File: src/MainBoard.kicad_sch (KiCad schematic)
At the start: 75 parts, among them J10 1217080-1, J11 1217080-1, J12 1217080-1, J13 1217080-1, J14 1217080-1, J15 1217080-1, J16 1217080-1, J4 MiniFit_2x08_F, J5 1217080-1, J6 1217080-1, J7 1217080-1, J8 1217080-1, J9 1217080-1, K1 RAYEX-L90S, K2 LR2A-12W, K3 LR2A-12W, Q1 BC547, Q10 2N7002, Q3 2N7002, Q4 2N7002, Q5 2N7002, Q6 2N7002, Q7 BC547, Q8 BC557, Q9 2N7002, U1 ATtiny85-20P

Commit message: Update schematics
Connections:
- new net: A1.6 (SS), A2.6 (SS)
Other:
- moved on the sheet: D4, D6, Q3, Q4, R?

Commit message: update Schematics
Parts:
- removed A1: MP2307DN_3A_Master, symbol Modules:MP2307DN_3A
- removed A2: MP2307DN_3A_Slave, symbol Modules:MP2307DN_3A
- removed A3: MP2307DN_3A, symbol Modules:MP2307DN_3A
- removed BT1: 8.4V, symbol Device:Battery_Cell
- removed C4, C5: 1µF, symbol Device:C_Polarized
- removed C6, C7: 2200µF, symbol Device:C_Polarized
- removed C? (x2): 120µF, Capacitor_THT:C_Disc_D5.0mm_W2.5mm_P5.00mm, symbol Device:C
- removed C?: 100nF, Capacitor_THT:C_Disc_D5.0mm_W2.5mm_P5.00mm, symbol Device:C
- removed D25, D8: US1M, Diode_SMD:D_SMA, symbol Diode:US1M
- removed D26, D6, D7: BZX79C2V7, Diode_SMD:D_MiniMELF, symbol Diode:BZV55C2V7
- removed F?: 12V 5A, symbol Device:Fuse
- removed F?: 12V 30A, symbol Device:Fuse
- removed F?: 12V 20A, symbol Device:Fuse
- removed F?: 12V 15A, symbol Device:Fuse
- removed F?: 12V 10A, symbol Device:Fuse
- removed F?: 5V 5A, symbol Device:Fuse
- removed J10, J11, J12, J13, J14, J15, J16, J5, J6, J7, J8, J9: 1217080-1, 1217080-1, symbol SamacSys_Parts:1217080-1
- removed J4: MiniFit_2x08_F, Connector_Molex:Molex_Mini-Fit_Jr_5566-16A_2x08_P4.20mm_Vertical, symbol Connector_Generic:Conn_02x08_Counter_Clockwise
- removed J?: Barrel_Jack, Connector_BarrelJack:BarrelJack_CUI_PJ-063AH_Horizontal, symbol Connector:Barrel_Jack
- removed J?: XT60-M, Connector_AMASS:AMASS_XT60PW-M_1x02_P7.20mm_Horizontal, symbol Connector:Conn_01x02_Pin
- removed J?: XT60L-F, Connector_AMASS:AMASS_XT60-M_1x02_P7.20mm_Vertical, symbol Connector:Conn_01x02_Pin
- removed K1: RAYEX-L90S, Relay_THT:Relay_SPDT_RAYEX-L90S, symbol Relay:RAYEX-L90S
- removed K2: LR2A-12W, SamacSys_Parts:AZ9431CH12DE, symbol Local Components:LR2A-12W
- removed K3: LR2A-12W, Relay_THT:Relay_SPDT_Finder_36.11, symbol Local Components:LR2A-12W
- removed L1, L2: 100µH, symbol Device:L_Ferrite
- removed Q1, Q7: BC547, Package_TO_SOT_THT:TO-92_Inline, symbol Transistor_BJT:BC547
- removed Q3, Q6: 2N7002, Package_TO_SOT_SMD:SOT-23, symbol Transistor_FET:2N7002
- removed Q8: BC557, Package_TO_SOT_THT:TO-92_Inline, symbol Transistor_BJT:BC557
- removed Q?: BPW96B, LED_THT:LED_D5.0mm, symbol Device:Q_Photo_NPN
- removed R? (x7): 10K, Resistor_SMD:R_1206_3216Metric_Pad1.30x1.75mm_HandSolder, symbol Device:R
- removed R? (x2): 33K, Resistor_SMD:R_1206_3216Metric_Pad1.30x1.75mm_HandSolder, symbol Device:R
- removed R?: 1K, Resistor_THT:R_Axial_DIN0204_L3.6mm_D1.6mm_P5.08mm_Horizontal, symbol Device:R
- removed R?: 1M, Resistor_SMD:R_1206_3216Metric_Pad1.30x1.75mm_HandSolder, symbol Device:R
- removed RV2: 47K, symbol Device:R_Potentiometer
- removed U1: ATtiny85-20P, Package_DIP:DIP-8_W7.62mm, symbol MCU_Microchip_ATtiny:ATtiny85-20P
- added C1: 10nF, symbol Device:C_Polarized
- added C2: 100nF, symbol Device:C_Polarized
- added D11, D7: P600A, Diode_THT:D_P600_R-6_P12.70mm_Horizontal, symbol Device:D
- added D23, D31, D32, D33, D5, D8: BZX79C2V7, Diode_SMD:D_MiniMELF, symbol Diode:BZV55C2V7
- added D6: US1M, Diode_SMD:D_SMA, symbol Diode:US1M
- added J3: MiniFit_2x10_F, symbol Connector_Generic:Conn_02x10_Counter_Clockwise
- added J69: 1217080-1, 1217080-1, symbol SamacSys_Parts:1217080-1
- added J?: XT60-M, Connector_AMASS:AMASS_XT60PW-M_1x02_P7.20mm_Horizontal, symbol Connector:Conn_01x02_Pin
- added J?: XT60L-F, Connector_AMASS:AMASS_XT60-M_1x02_P7.20mm_Vertical, symbol Connector:Conn_01x02_Pin
- added K4 (x2): FINDER-40.61, Relay_THT:Relay_DPDT_Finder_40.52, symbol Relay:FINDER-40.51
- added Q1, Q11, Q13, Q2: 2N7002, Package_TO_SOT_SMD:SOT-23, symbol Transistor_FET:2N7002
- added Q12, Q3: BS250, Package_TO_SOT_THT:TO-92_Inline, symbol Transistor_FET:BS250
- added R? (x7): 10K, Resistor_SMD:R_1206_3216Metric_Pad1.30x1.75mm_HandSolder, symbol Device:R
- added R?: 1K, Resistor_SMD:R_1206_3216Metric_Pad1.30x1.75mm_HandSolder, symbol Device:R
- added U1: LM555xN, Package_DIP:DIP-8_W7.62mm, symbol Timer:LM555xN
- RV1: value 100K -> 10K-50K
- renumbered D5 to D12
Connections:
- net +5V: now also J3.6 (Pin_6), R?.2, U1.8 (VCC); no longer RV1.1
- net +BATT: now also J3.7 (Pin_7), Q12.1 (D), Q3.1 (D); no longer D3.1 (K)
- net +VDC: now also J?.2 (Pin_2), J?.2 (Pin_2)
- net GND: now also C1.2, C2.2, D23.2 (A), D31.2 (A), D33.2 (A), D5.2 (A), D8.2 (A), J69.1, J69.2, J?.1 (Pin_1), J?.1 (Pin_1), K4.12, K4.12, Q1.2 (S), Q11.2 (S), Q13.2 (S), Q2.2 (S), U1.1 (GND); no longer D10.2 (A), D2.2 (A), D9.2 (A), Q10.2 (S), Q9.2 (S), RV1.3
- net GNDDash: now also Q10.2 (S), J3.8 (Pin_8)
- net Key: now also J3.1 (Pin_1)
- net LowBat: now also J3.10 (Pin_10)
- net PLight: now also J3.9 (Pin_9), R?.1
- net VInst: now also J3.3 (Pin_3)
- net VLight: now also J3.5 (Pin_5), K4.14, K4.14
- net VOutlet: now also J3.4 (Pin_4)
- net VRadio: now also J3.2 (Pin_2)
- net at Q4.1 (G): now also D8.1 (K), Q3.2 (G), R?.2
- net at Q4.3 (D): now also Q3.3 (S), R?.1
- net PLightSignal: now reaches Q10.1 (G)
- net PLightSignal: now also D32.1 (K), Q12.2 (G), Q13.1 (G), R?.2, U1.4 (R)
- net at Q9.1 (G): now also D23.1 (K), R?.2; no longer Q10.3 (D)
- net AuxHBeam: now reaches D3.2 (A)
- net AuxHBeam: now also J3.13 (Pin_13), K4.11
- net at D12.1 (K), Q5.1 (G), R?.2: now also R?.2
- net at RV1.2: now also C2.1, U1.2 (TR), U1.6 (THR)
- net at D4.1 (K): now also Q1.1 (G), R?.2
- net at D1.2 (A): now also K4.A2, Q1.3 (D)
- net HazardLed: now reaches Q9.3 (D)
- net HazardLed: now also J3.17 (Pin_17), Q11.3 (D)
- net +5VA renamed AuxSwitch
- net AuxSwitch: now also J3.16 (Pin_16), K4.A1, K4.A1
- net AuxSwitch1: no longer names the net of D9.1 (K)
- net AuxSwitch1: now also RV1.3
- net AuxSwitch2: no longer names the net of D10.1 (K)
- net AuxSwitch2: now also D9.2 (A), R?.1, U1.7 (DIS)
- net DimmerDash: no longer names the net of R?.1
- net DimmerDash: now also R?.1, U1.3 (Q)
- new net: D2.2 (A), K4.A2, Q2.3 (D)
- new net: D32.2 (A), D33.1 (K)
- new net: Q12.3 (S), Q13.3 (D), R?.1
- new net: D31.1 (K), Q11.1 (G), R?.2
- new net: D5.1 (K), Q2.1 (G), R?.2
- new net: C1.1, U1.5 (CV)
- new net: D10.2 (A), RV1.1
- new net: Q10.3 (D), Q9.2 (S)
- new net AuxBeams: D3.1 (K), D6.1 (K), J3.15 (Pin_15)
- new net AuxLBeam: D6.2 (A), J3.11 (Pin_11), K4.11
- new net HBeam: J3.14 (Pin_14), R?.1
- new net Hazard: D11.2 (A), D7.2 (A), J3.18 (Pin_18), R?.1
- new net LBeam: J3.12 (Pin_12), R?.1
- new net LBlinker: D11.1 (K), J3.19 (Pin_19)
- new net RBlinker: D7.1 (K), J3.20 (Pin_20)
- no-connect marks 4 -> 0
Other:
- added sheet Power Delivery (FuseBox.kicad_sch)
- note added: "Common Ground"
- note added: "Hazard signal"
- note added: "Main Power"
- note removed: "12DC Outlet"
- note removed: "CLC Choke"
- note removed: "Fuse Box"
- note removed: "Low Battery meter (Set trigger at > 11.5V)"
- note removed: "Main Power and Kill switch"
- note removed: "Radio backup battery"
- note removed: "Voltage Regulator (5V, 6A Max) Remove FB, SS and Comp circuitry from Slave module Jumper wire both modules chip"
- moved on the sheet: D12, Q5, R?

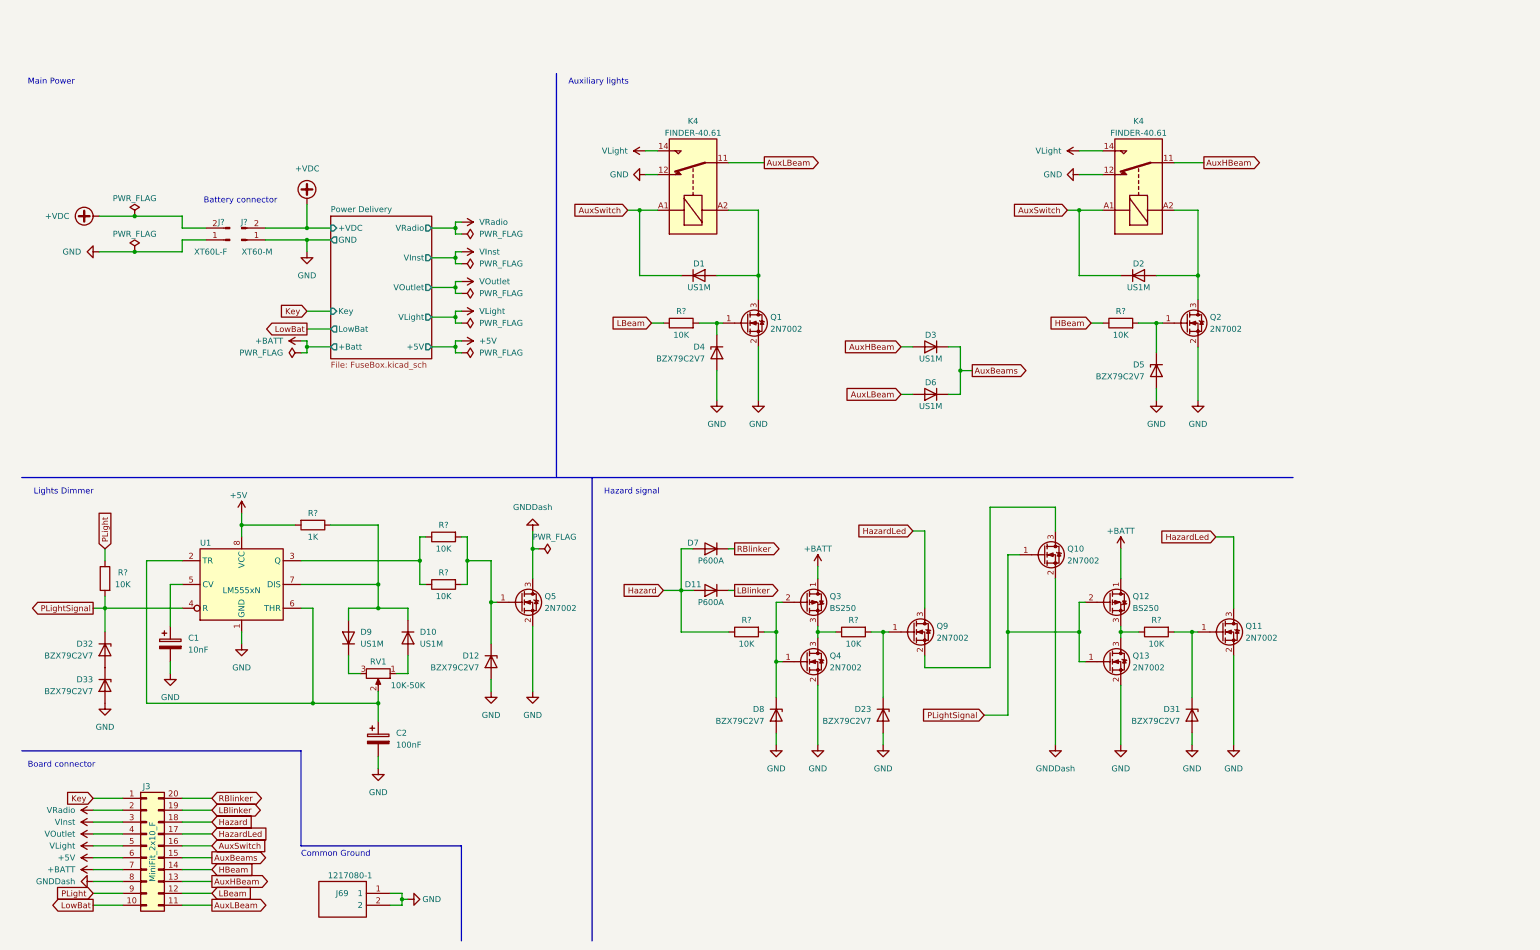
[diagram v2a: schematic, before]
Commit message: Update Schmatics; Cleanup unecessary circuits; Simplify blinkers dimmers; Update PCB; Colorize motorcycle electric diagram.
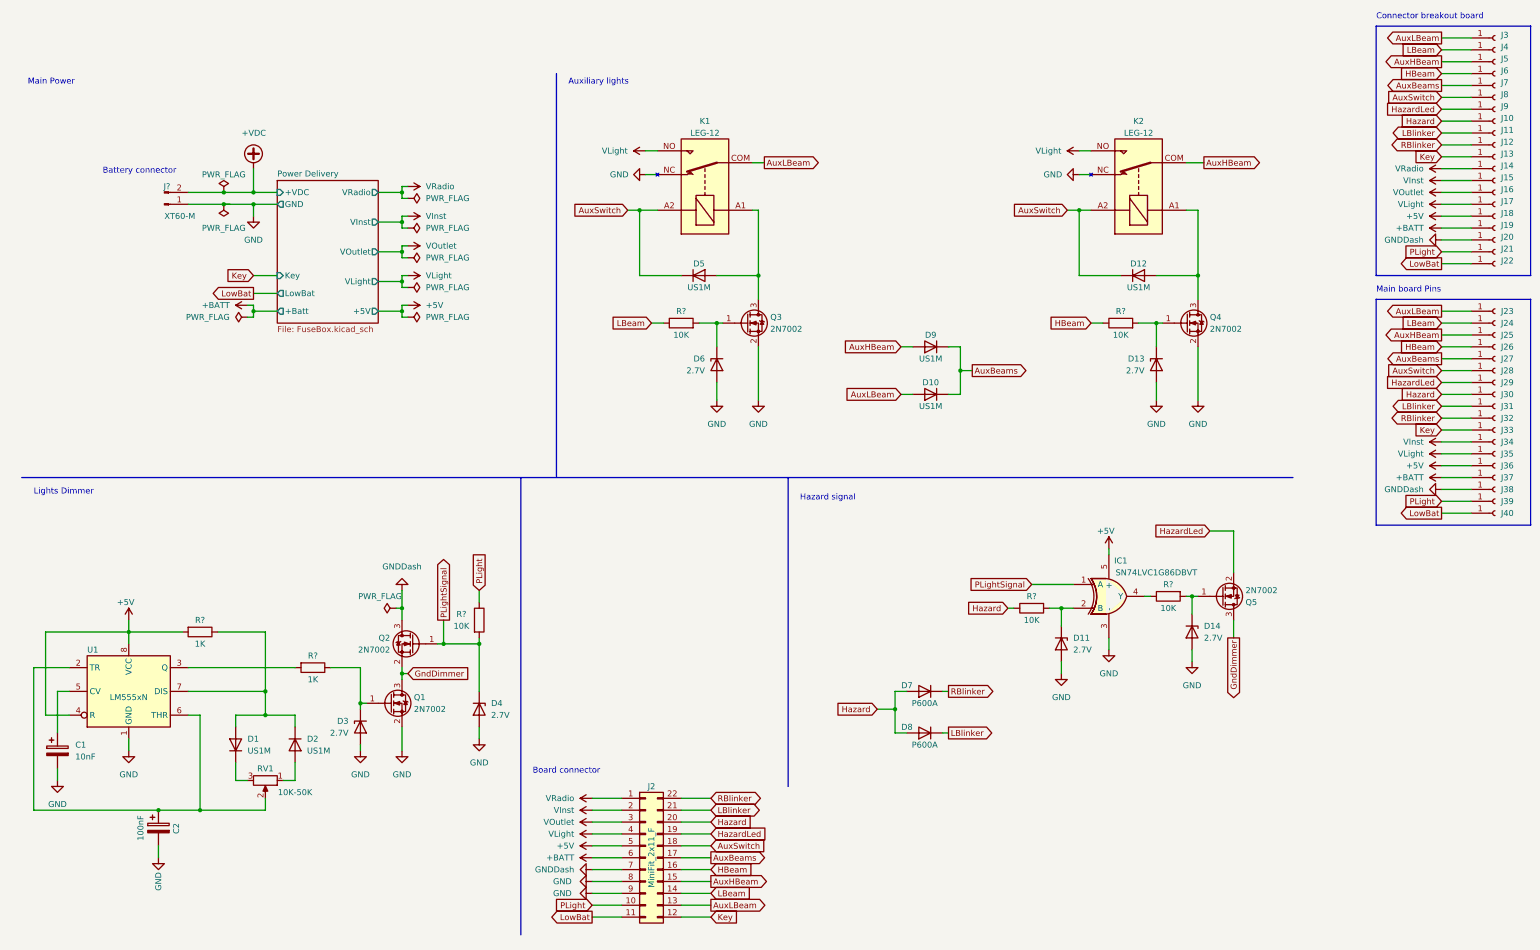
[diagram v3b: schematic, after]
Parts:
- removed D12, D23, D31, D32, D33, D5, D8: BZX79C2V7, Diode_SMD:D_MiniMELF, symbol Diode:BZV55C2V7
- removed J3: MiniFit_2x10_F, symbol Connector_Generic:Conn_02x10_Counter_Clockwise
- removed J69: 1217080-1, 1217080-1, symbol SamacSys_Parts:1217080-1
- removed J?: XT60L-F, Connector_AMASS:AMASS_XT60-M_1x02_P7.20mm_Vertical, symbol Connector:Conn_01x02_Pin
- removed K4 (x2): FINDER-40.61, Relay_THT:Relay_DPDT_Finder_40.52, symbol Relay:FINDER-40.51
- removed Q10, Q11, Q13, Q4, Q9: 2N7002, Package_TO_SOT_SMD:SOT-23, symbol Transistor_FET:2N7002
- removed Q12, Q3: BS250, Package_TO_SOT_THT:TO-92_Inline, symbol Transistor_FET:BS250
- removed R? (x5): 10K, Resistor_SMD:R_1206_3216Metric_Pad1.30x1.75mm_HandSolder, symbol Device:R
- added D11, D13, D14, D3, D4: 2.7V, Diode_SMD:D_MiniMELF, symbol Diode:BZV55C2V7
- added IC1: SN74LVC1G86DBVT, SOT95P280X145-5N, symbol Local Components:SN74LVC1G86DBVT
- added J10, J11, J12, J13, J14, J15, J16, J17, J18, J19, J20, J21, J22, J23, J24, J25, J26, J27, J28, J29, J3, J30, J31, J32, J33, J34, J35, J36, J37, J38, J39, J4, J40, J5, J6, J7, J8, J9: Conn_01x01_Socket, Connector_Pin:Pin_D1.0mm_L10.0mm, symbol Connector:Conn_01x01_Socket
- added J2: MiniFit_2x11_F, symbol Connector_Generic:Conn_02x11_Counter_Clockwise
- added K1, K2: LEG-12, Local Footprints:LEG12, symbol Local Components:LEG-12
- added Q2, Q5: 2N7002, Package_TO_SOT_SMD:SOT-23, symbol Transistor_FET:2N7002
- added R?: 1K, Resistor_SMD:R_1206_3216Metric_Pad1.30x1.75mm_HandSolder, symbol Device:R
- added R? (x2): 10K, Resistor_SMD:R_1206_3216Metric_Pad1.30x1.75mm_HandSolder, symbol Device:R
- D6: renamed from D4; value BZX79C2V7 -> 2.7V
- J?: footprint Connector_AMASS:AMASS_XT60PW-M_1x02_P7.20mm_Horizontal -> Local Footprints:AMASS_XT60PW-M_1x02_P7.20mm_Horizontal_Short
- renumbered D9 to D1, D6 to D10, D2 to D12, D10 to D2, D1 to D5, D11 to D8, D3 to D9, Q5 to Q1, Q1 to Q3, Q2 to Q4
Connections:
- net +5V: now also U1.4 (R), IC1.5 (+), J18.1 (Pin_1), J2.5 (Pin_5), J36.1 (Pin_1)
- net +BATT: now also J19.1 (Pin_1), J2.6 (Pin_6), J37.1 (Pin_1)
- net AuxBeams: now also J2.17 (Pin_17), J27.1 (Pin_1), J7.1 (Pin_1)
- net AuxHBeam: now also J2.15 (Pin_15), J25.1 (Pin_1), J5.1 (Pin_1), K2.COM
- net AuxLBeam: now also J2.13 (Pin_13), J23.1 (Pin_1), J3.1 (Pin_1), K1.COM
- net AuxSwitch: now also J2.18 (Pin_18), J28.1 (Pin_1), J8.1 (Pin_1), K1.A2, K2.A2
- net GND: now also D11.2 (A), D13.2 (A), D14.2 (A), D3.2 (A), D4.2 (A), IC1.3 (-), J2.8 (Pin_8), J2.9 (Pin_9), K1.NC, K2.NC
- net GNDDash: now also J2.7 (Pin_7), J20.1 (Pin_1), J38.1 (Pin_1), Q2.3 (D); no longer Q1.3 (D)
- net HBeam: now also J2.16 (Pin_16), J26.1 (Pin_1), J6.1 (Pin_1)
- net Hazard: now also J10.1 (Pin_1), J2.20 (Pin_20), J30.1 (Pin_1), R?.1
- net HazardLed: now also J2.19 (Pin_19), J29.1 (Pin_1), J9.1 (Pin_1), Q5.2 (S)
- net Key: now also J13.1 (Pin_1), J2.12 (Pin_12), J33.1 (Pin_1)
- net LBeam: now also J2.14 (Pin_14), J24.1 (Pin_1), J4.1 (Pin_1)
- net LBlinker: now also J11.1 (Pin_1), J2.21 (Pin_21), J31.1 (Pin_1)
- net LowBat: now also J2.11 (Pin_11), J22.1 (Pin_1), J40.1 (Pin_1)
- net PLight: now also J2.10 (Pin_10), J21.1 (Pin_1), J39.1 (Pin_1)
- net PLightSignal: now also D4.1 (K), IC1.1 (A), Q2.1 (G); no longer U1.4 (R)
- net RBlinker: now also J12.1 (Pin_1), J2.22 (Pin_22), J32.1 (Pin_1)
- net VInst: now also J15.1 (Pin_1), J2.2 (Pin_2), J34.1 (Pin_1)
- net VLight: now also J17.1 (Pin_1), J2.4 (Pin_4), J35.1 (Pin_1), K1.NO, K2.NO
- net VOutlet: now also J16.1 (Pin_1), J2.3 (Pin_3)
- net VRadio: now also J14.1 (Pin_1), J2.1 (Pin_1)
- net at D12.2 (A), Q4.3 (D): now also K2.A1
- net at U1.3 (Q): now also R?.2
- net at Q1.1 (G): now also D3.1 (K), R?.1
- net at Q4.1 (G), R?.2: now also D13.1 (K)
- net at D5.2 (A), Q3.3 (D): now also K1.A1
- new net: D14.1 (K), Q5.1 (G), R?.2
- new net: D11.1 (K), IC1.2 (B), R?.2
- new net: IC1.4 (Y), R?.1
- new net GndDimmer: Q1.3 (D), Q2.2 (S), Q5.3 (D)
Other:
- note added: "Connector breakout board"
- note added: "Main board Pins"
- note removed: "Common Ground"
- moved on the sheet: C1, C2, D1, D2, D6, D7, D8, J?, Q1, R?, RV1, U1

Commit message: Update Schematics; Replace xor with quad nand; Update PCB
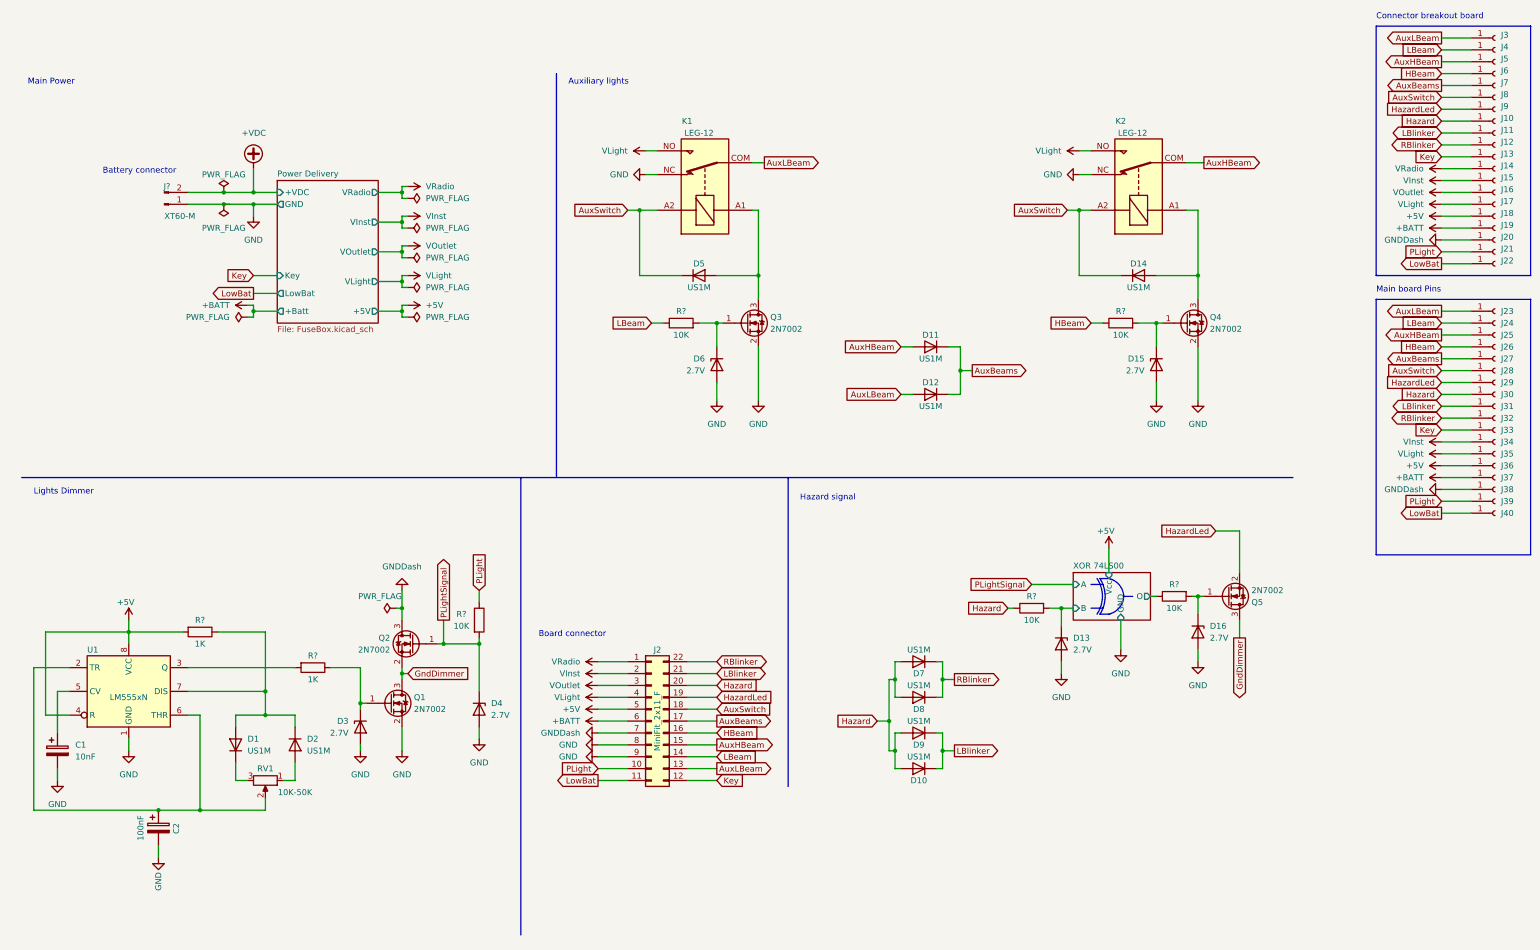
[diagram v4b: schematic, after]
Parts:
- removed D7, D8: P600A, Diode_THT:D_P600_R-6_P12.70mm_Horizontal, symbol Device:D
- removed IC1: SN74LVC1G86DBVT, SOT95P280X145-5N, symbol Local Components:SN74LVC1G86DBVT
- added D10, D7, D8, D9: US1M, Diode_SMD:D_SMA, symbol Diode:US1M
- U1: footprint Package_DIP:DIP-8_W7.62mm -> Package_DIP:DIP-8_W7.62mm_Socket_LongPads
- renumbered D9 to D11, D10 to D12, D11 to D13, D12 to D14, D13 to D15, D14 to D16
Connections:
- net Hazard: now also D10.2 (A), D7.2 (A), D8.2 (A), D9.2 (A)
- net LBlinker: now also D10.1 (K), D9.1 (K)
- net RBlinker: now also D7.1 (K), D8.1 (K)
- net XOR 74LS00/B: now reaches D13.1 (K), R?.2
- net XOR 74LS00/O: now reaches R?.1
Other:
- added sheet XOR 74LS00 (XOR 74LS00.kicad_sch)
- moved on the sheet: D16, J2, Q5, R?
